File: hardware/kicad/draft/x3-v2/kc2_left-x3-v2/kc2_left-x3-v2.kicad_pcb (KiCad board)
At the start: 2 copper layers, 135.1 x 122.5 mm, 73 parts, among them SW1 KEY_01, SW10 KEY_10, SW11 KEY_11, SW12 KEY_12, SW13 KEY_13, SW14 KEY_14, SW15 KEY_15, SW16 KEY_16, SW17 KEY_17, SW18 KEY_18, SW19 KEY_19, SW2 KEY_02, SW20 KEY_20, SW21 KEY_21, SW22 KEY_22, SW23 KEY_23, SW24 KEY_24, SW25 KEY_25, SW26 KEY_26, SW27 KEY_27, SW28 KEY_28, SW29 KEY_29, SW3 KEY_03, SW30 KEY_30, SW31 KEY_31, SW4 KEY_04, SW5 KEY_05, SW6 KEY_06, SW7 KEY_07, SW8 KEY_08, SW9 KEY_09, U1 nice!nano_v2_socket_24pin

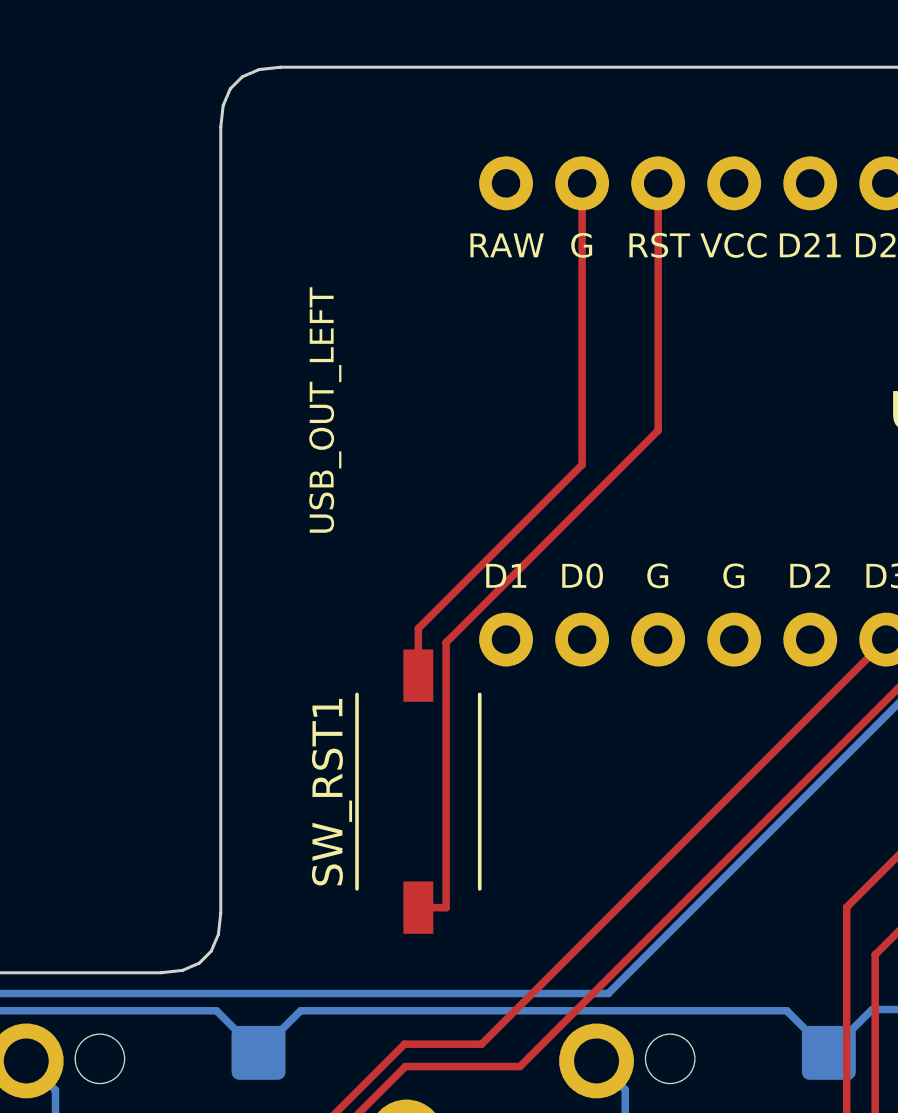
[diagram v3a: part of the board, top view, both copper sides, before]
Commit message: feat(x3-v2): USB 하부 리셋 배치와 실크 충돌 수정
소켓으로 높아진 nice!nano 아래 공간을 활용하도록 좌우 리셋 배치와 RST/GND 라우팅을 재구성한다. 우측 Reference 필드를 안전한 위치로 옮겨 DRC 경고를 제거하고 SRS, 해시 증거, 생성·검증 코드를 갱신한다.

Requirements: CON-ARCH-004, CON-ARCH-006, OPS-ARCH-003
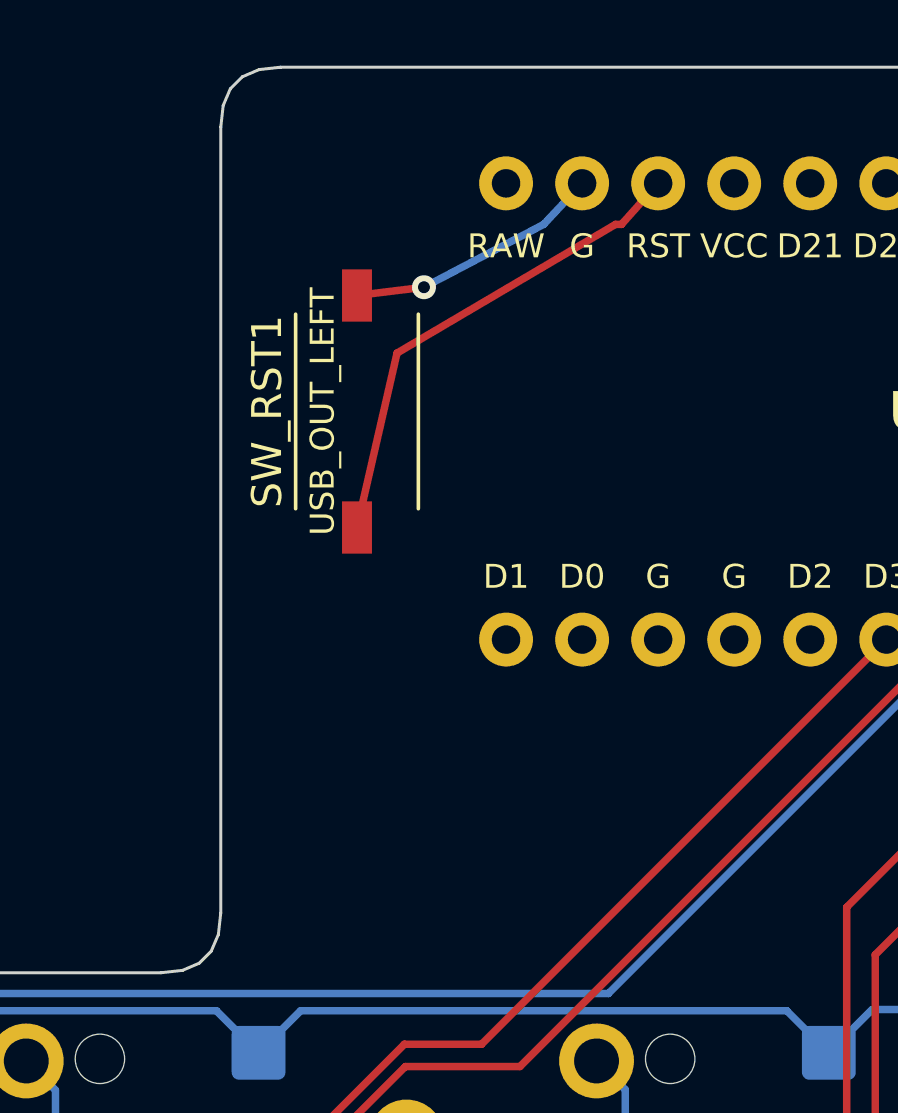
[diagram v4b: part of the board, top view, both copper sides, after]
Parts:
- moved SW_RST1 12.9 mm to (113.8, 50.8)
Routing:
- net RST: track 28.1 -> 16.5 mm
- net GND: track 18.7 -> 8.65 mm, vias 0 -> 1
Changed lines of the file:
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@@
 	(footprint "SW_NW3_A06_B3_SMD"
 		(layer "F.Cu")
-		(at 115.8125 63.45 90)
+		(at 113.7625 50.75 90)
 		(descr "Microstack NW3-A06-B3 micro tact switch, SMD, 6.1 x 3.7 mm body, 2.55 mm height, DeviceMart no.1322056")
 		(tags "switch tactile SPST SMD NW3-A06-B3")
@@
 	)
 	(segment
-		(start 121.2825 52.5287)
-		(end 115.8125 57.9987)
+		(start 113.7625 46.875)
+		(end 116 46.6)
 		(width 0.25)
 		(layer "F.Cu")
 		(net "GND")
 	)
+	(via
+		(at 116 46.6)
+		(size 0.8)
+		(drill 0.4)
+		(layers "F.Cu" "B.Cu")
+		(net "GND")
+	)
 	(segment
-		(start 115.8125 57.9987)
-		(end 115.8125 59.575)
+		(start 120 44.5)
+		(end 121.2825 43.13)
 		(width 0.25)
-		(layer "F.Cu")
+		(layer "B.Cu")
 		(net "GND")
 	)
 	(segment
-		(start 121.2825 43.13)
-		(end 121.2825 52.5287)
+		(start 116 46.6)
+		(end 120 44.5)
 		(width 0.25)
-		(layer "F.Cu")
+		(layer "B.Cu")
 		(net "GND")
 	)
 	(segment
-		(start 116.7392 58.4698)
-		(end 123.8225 51.3865)
+		(start 115.1 48.8)
+		(end 122.4 44.5)
 		(width 0.25)
 		(layer "F.Cu")
@@
 	)
 	(segment
-		(start 116.7392 67.325)
-		(end 116.7392 58.4698)
+		(start 113.7625 54.625)
+		(end 115.1 48.8)
 		(width 0.25)
 		(layer "F.Cu")
@@
 	)
 	(segment
-		(start 123.8225 51.3865)
+		(start 122.6 44.5)
 		(end 123.8225 43.13)
 		(width 0.25)
@@
 	)
 	(segment
-		(start 115.8125 67.325)
-		(end 116.7392 67.325)
+		(start 122.4 44.5)
+		(end 122.6 44.5)
 		(width 0.25)
 		(layer "F.Cu")

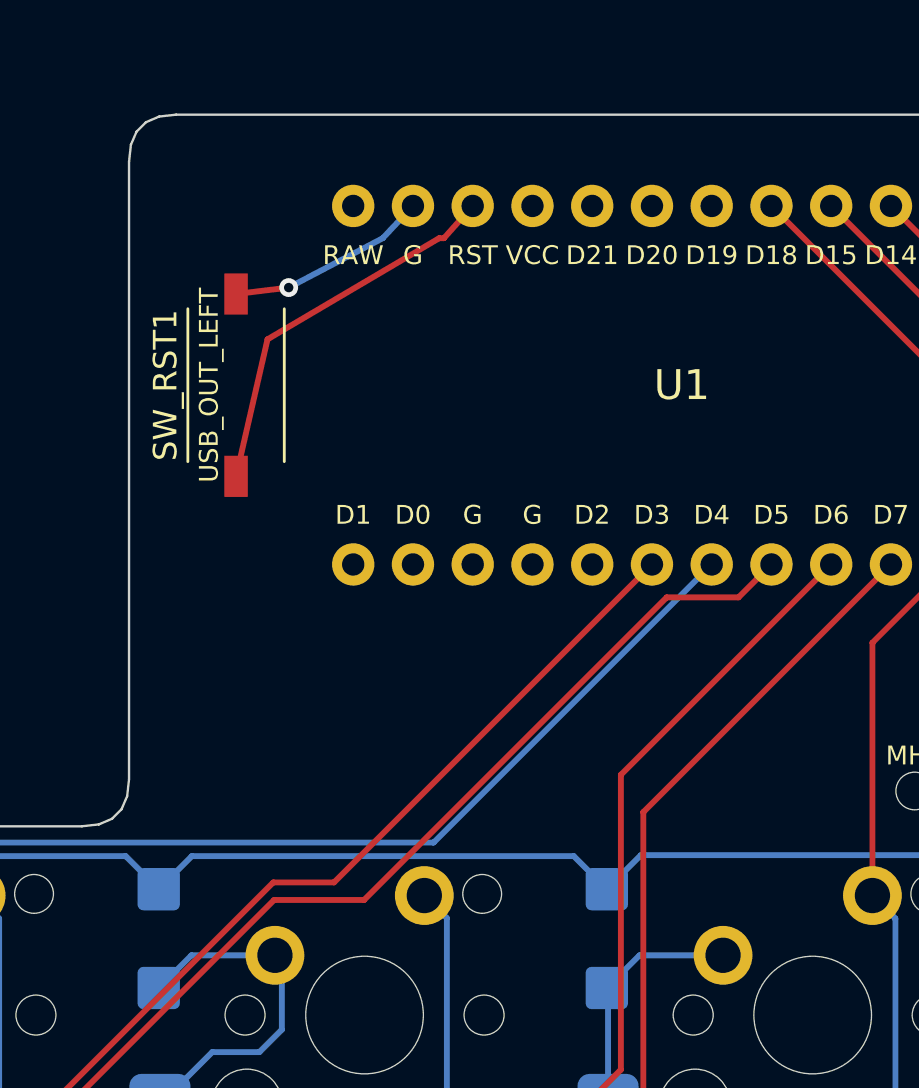
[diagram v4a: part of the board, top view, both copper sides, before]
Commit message: feat(x3-v2): add switched battery service layout
- Add direct-solder battery power and mirrored power/reset controls.
- Integrate controller-service openings and lower-housing support.
- Regenerate routing, DRC, fabrication, mechanical, render, and model evidence.
- Document protected KiCad mutations and keep physical gates order-blocked.

Refs: CON-ARCH-004
Refs: CON-ARCH-006
Refs: CON-ARCH-007
Refs: REL-ARCH-001
Refs: OPS-ARCH-003
Refs: OPS-ARCH-004
Refs: OPS-ARCH-005
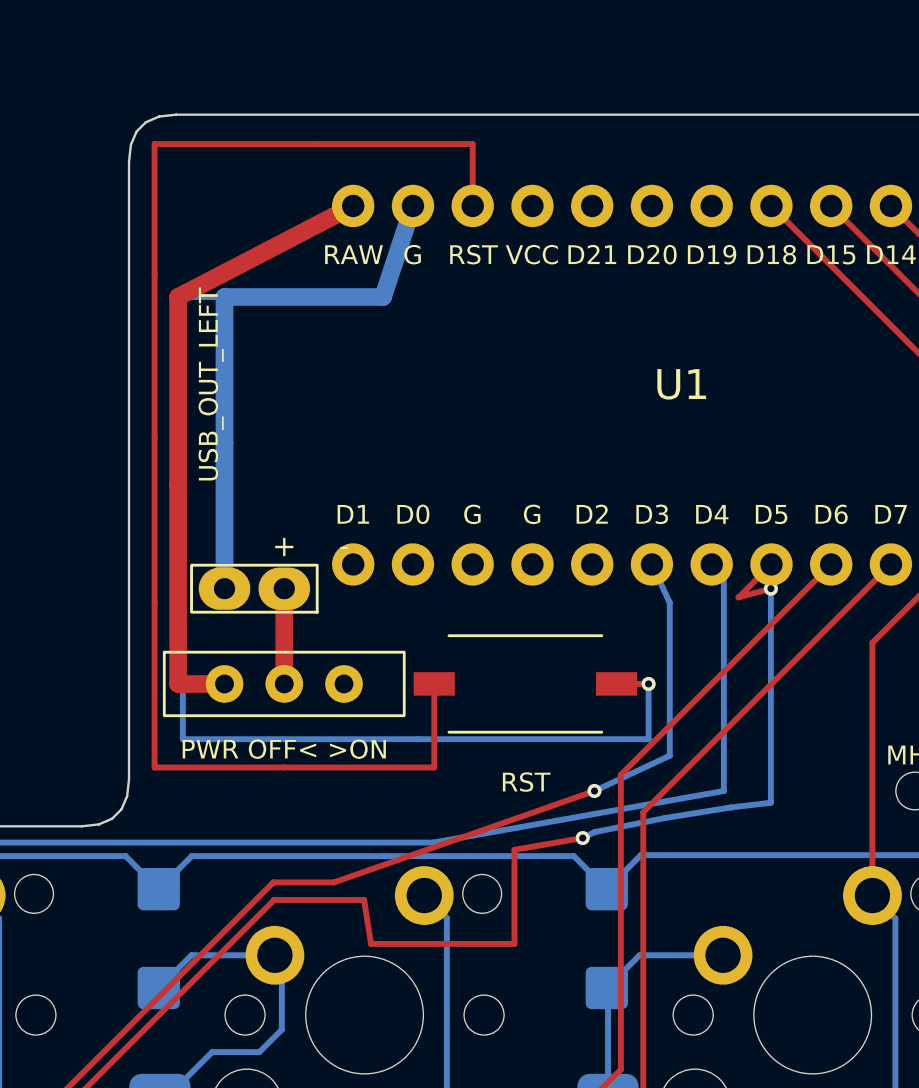
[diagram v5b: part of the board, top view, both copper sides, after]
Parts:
- added BAT1: BAT_301230_30x12mm, KC2:BAT_301230_30x12mm, F.Cu at (131.7, 50.8)
- added J_BAT1: BAT_2Pin_PTH_DirectSolder, KC2:BAT_2Pin_PTH_DirectSolder, F.Cu at (115.8, 59.4)
- added SW_PWR1: SW_IMMS_12V_BSI10_THT, KC2:SW_IMMS_12V_BSI10_THT, F.Cu at (115.8, 63.5)
- moved SW_RST1 17.7 mm to (126.1, 63.5), turned to 0 degrees
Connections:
- U1 pad RAW: (no net) -> NN_B+
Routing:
- net GND: track 8.65 -> 67.3 mm
- net RST: track 16.5 -> 58.1 mm
- net NN_B+: track 0.00 -> 26.8 mm
- net L_COL1: track 232.6 -> 245.0 mm, vias 2 -> 4
- net L_COL2: track 176.0 -> 181.6 mm
- net L_COL0: track 236.3 -> 240.7 mm, vias 1 -> 2
- net BAT+: track 0.00 -> 4.05 mm
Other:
- board text added: "+"
- board text added: "-"
- board text added: "BAT STRAIN RELIEF"
- board text added: "PWR OFF< >ON"
- board text added: "RST"
- board text removed: "BAT LEAD EXIT"
- board text removed: "Battery solders directly to nice!nano B+/B-; no carrier power pads"
- board text removed: "TW301525 80mAh"

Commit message: feat(x3-v2): finalize service controls and rounded mounts
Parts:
- moved MH5 11.0 mm to (124.7, 125.1)
- moved MH3 10.6 mm to (108.5, 87.0)
- moved MH4 0.30 mm to (57.4, 99.0)
- moved MH1 0.10 mm to (142.6, 67.9)
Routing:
- net L_COL4: track 172.9 -> 168.6 mm
- net L_COL3: track 166.2 -> 167.3 mm
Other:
- board text removed: "+"
- board text removed: "-"

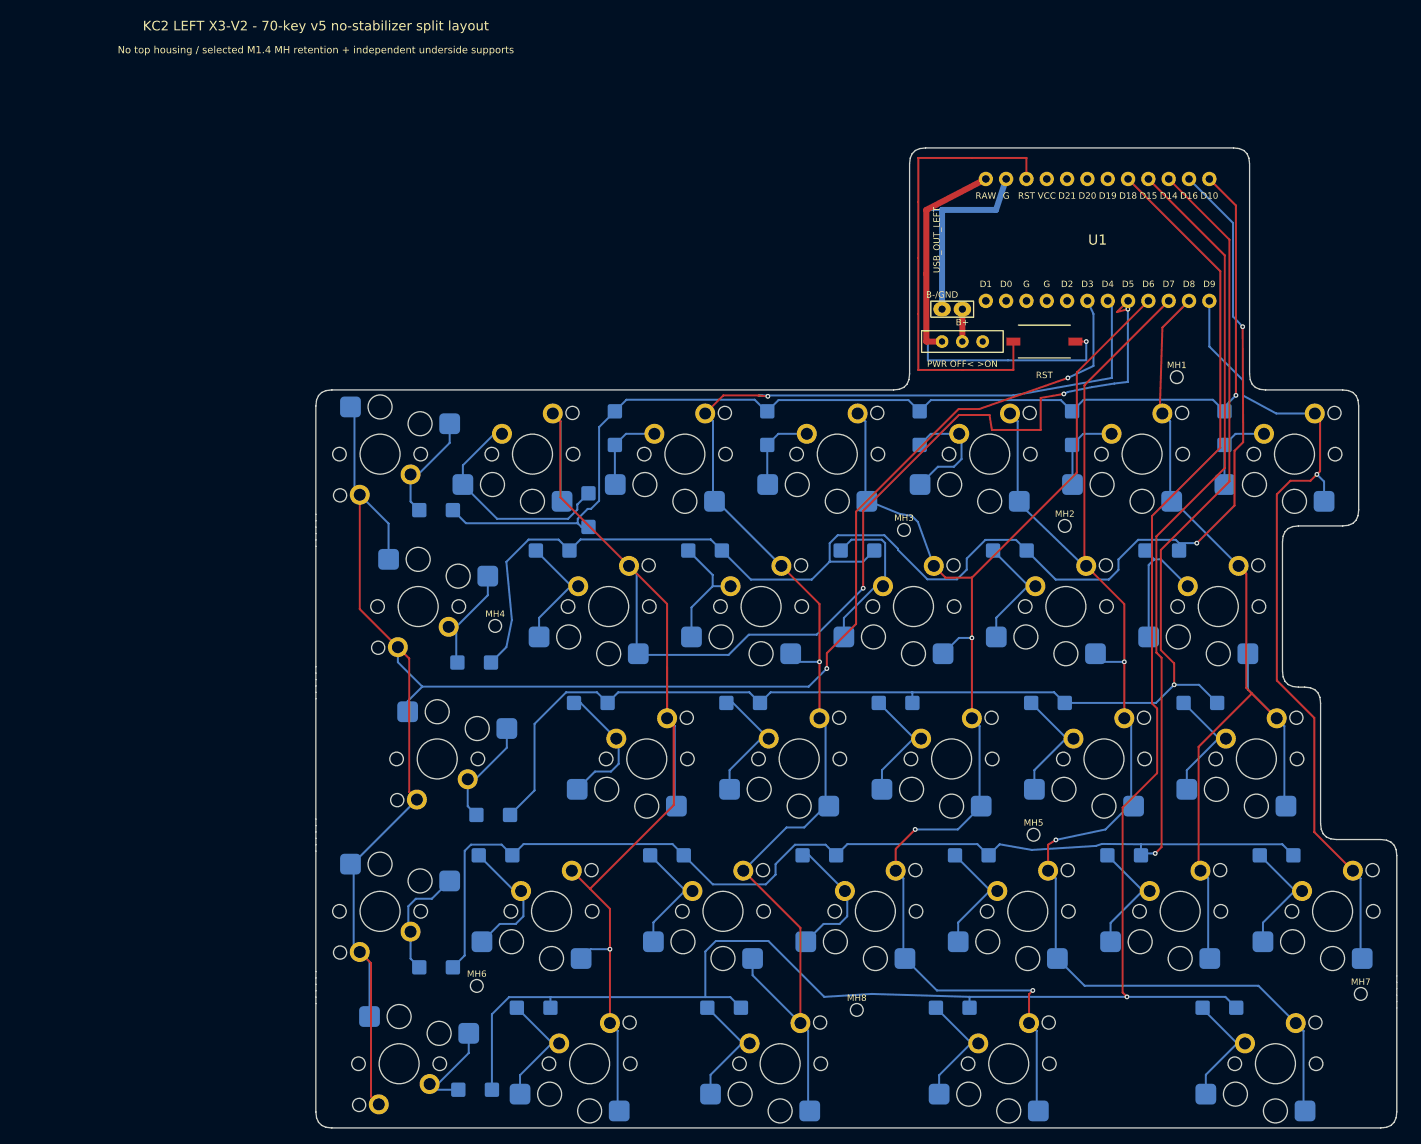
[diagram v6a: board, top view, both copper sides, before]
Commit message: wip(x3-v2): redesign mounts and per-key supports
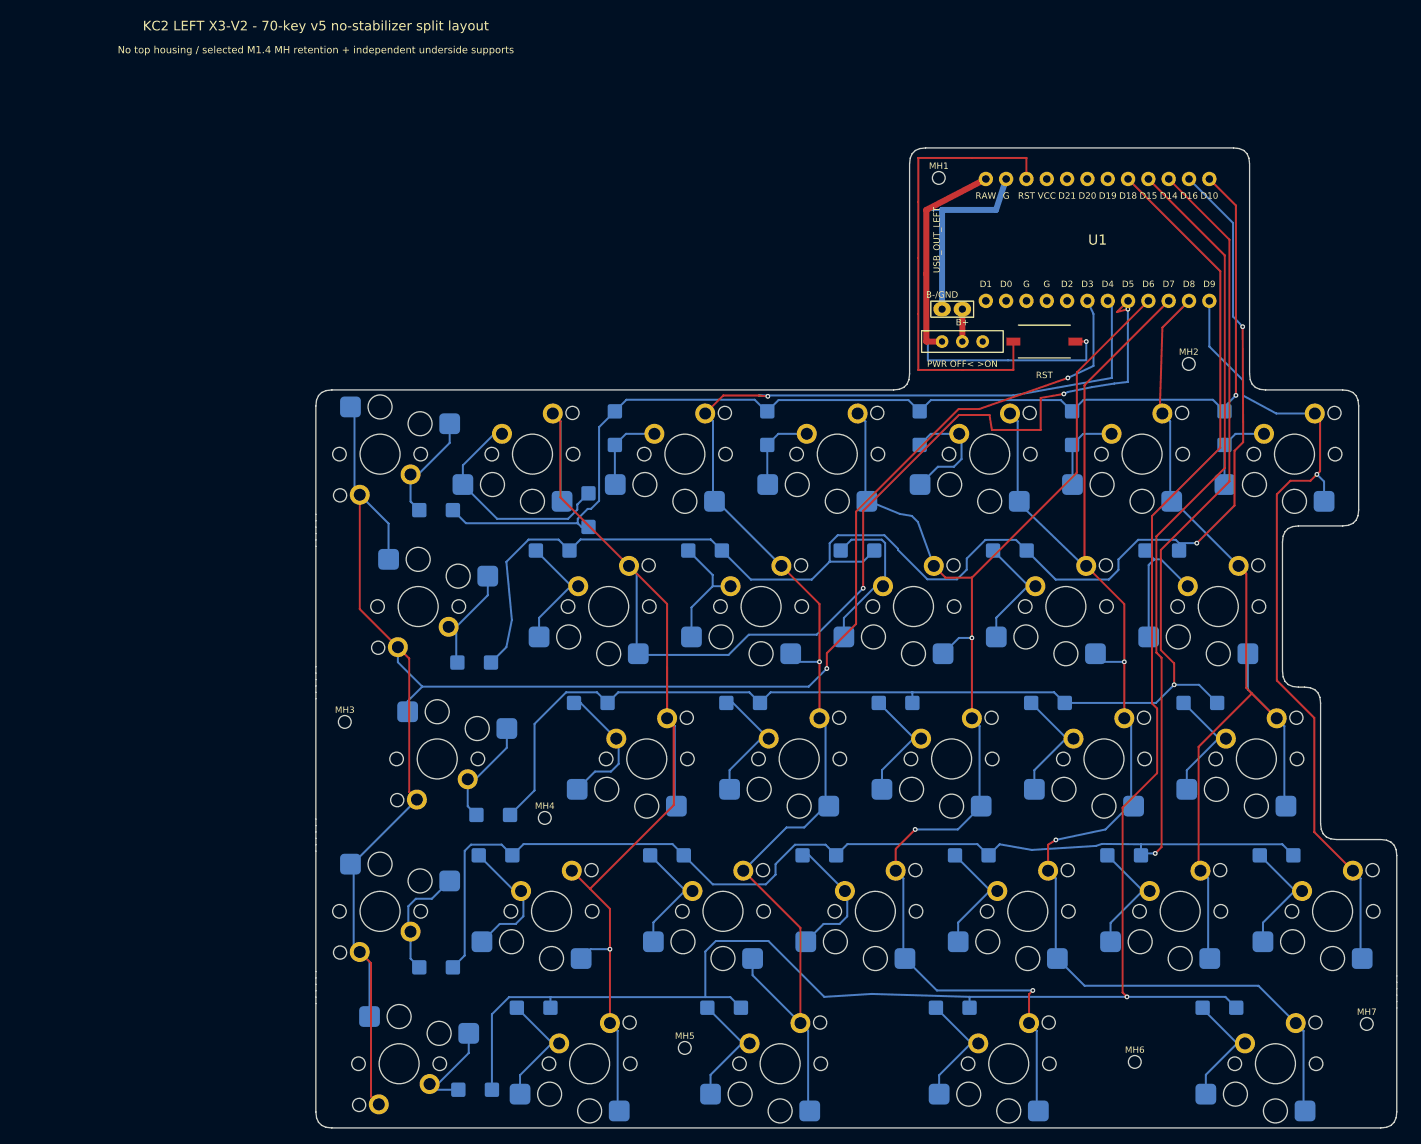
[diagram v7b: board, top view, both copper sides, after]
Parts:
- removed MH8: M1.4_NPTH_1.60, MH_M1.4_NPTH_1.60
- moved MH6 82.8 mm to (137.4, 153.5)
- moved MH3 73.9 mm to (38.6, 111.0)
- moved MH5 51.1 mm to (81.1, 151.8)
- moved MH1 38.8 mm to (112.9, 43.0)
- moved MH2 25.5 mm to (144.1, 66.2)
- moved MH4 24.8 mm to (63.6, 123.0)
- moved MH7 3.82 mm to (166.4, 148.8)
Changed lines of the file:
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@@
 	(footprint "MH_M1.4_NPTH_1.60"
 		(layer "F.Cu")
-		(at 124.7125 125.1)
+		(at 81.1125 151.75)
 		(descr "KC2 X3 V2 M1.4 service mounting hole, 1.60 mm copper-free NPTH")
 		(tags "KC2 X3 V2 M1.4 mounting NPTH copper-free")
@@
 	(footprint "MH_M1.4_NPTH_1.60"
 		(layer "F.Cu")
-		(at 142.6125 67.9)
+		(at 112.8625 43)
 		(descr "KC2 X3 V2 M1.4 service mounting hole, 1.60 mm copper-free NPTH")
 		(tags "KC2 X3 V2 M1.4 mounting NPTH copper-free")
@@
 	(footprint "MH_M1.4_NPTH_1.60"
 		(layer "F.Cu")
-		(at 57.4125 99)
+		(at 63.6125 123)
 		(descr "KC2 X3 V2 M1.4 service mounting hole, 1.60 mm copper-free NPTH")
 		(tags "KC2 X3 V2 M1.4 mounting NPTH copper-free")
@@
 	(footprint "MH_M1.4_NPTH_1.60"
 		(layer "F.Cu")
-		(at 102.6125 147)
-		(descr "KC2 X3 V2 M1.4 service mounting hole, 1.60 mm copper-free NPTH")
-		(tags "KC2 X3 V2 M1.4 mounting NPTH copper-free")
-		(property "Reference" "MH8"
-			(at 0 -1.5 0)
-			(layer "F.SilkS")
-			(effects
-				(font
-					(size 0.8 0.8)
-					(thickness 0.15)
-				)
-			)
-		)
-		(property "Value" "M1.4_NPTH_1.60"
-			(at 0 0 0)
-			(layer "F.Fab")
-			(hide yes)
-			(effects
-				(font
-					(size 0.8 0.8)
-					(thickness 0.1)
-				)
-			)
-		)
-		(property "Datasheet" ""
-			(at 0 0 0)
-			(layer "F.Fab")
-			(hide yes)
-			(effects
-				(font
-					(size 1.27 1.27)
-				)
-			)
-		)
-		(property "Description" ""
-			(at 0 0 0)
-			(layer "F.Fab")
-			(hide yes)
-			(effects
-				(font
-					(size 1.27 1.27)
-				)
-			)
-		)
-		(attr exclude_from_pos_files exclude_from_bom)
-		(duplicate_pad_numbers_are_jumpers no)
-		(pad "" np_thru_hole circle
-			(at 0 0)
-			(size 1.6 1.6)
-			(drill 1.6)
-			(layers "*.Mask")
-		)
-		(embedded_fonts no)
-	)
-	(footprint "MH_M1.4_NPTH_1.60"
-		(layer "F.Cu")
-		(at 128.6125 86.5)
+		(at 144.1125 66.25)
 		(descr "KC2 X3 V2 M1.4 service mounting hole, 1.60 mm copper-free NPTH")
 		(tags "KC2 X3 V2 M1.4 mounting NPTH copper-free")
@@
 	(footprint "MH_M1.4_NPTH_1.60"
 		(layer "F.Cu")
-		(at 55.1125 144)
+		(at 137.3625 153.5)
 		(descr "KC2 X3 V2 M1.4 service mounting hole, 1.60 mm copper-free NPTH")
 		(tags "KC2 X3 V2 M1.4 mounting NPTH copper-free")
@@
 	(footprint "MH_M1.4_NPTH_1.60"
 		(layer "F.Cu")
-		(at 165.6125 145)
+		(at 166.3625 148.75)
 		(descr "KC2 X3 V2 M1.4 service mounting hole, 1.60 mm copper-free NPTH")
 		(tags "KC2 X3 V2 M1.4 mounting NPTH copper-free")
@@
 	(footprint "MH_M1.4_NPTH_1.60"
 		(layer "F.Cu")
-		(at 108.5125 87)
+		(at 38.6125 111)
 		(descr "KC2 X3 V2 M1.4 service mounting hole, 1.60 mm copper-free NPTH")
 		(tags "KC2 X3 V2 M1.4 mounting NPTH copper-free")
